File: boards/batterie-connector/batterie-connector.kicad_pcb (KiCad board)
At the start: 2 copper layers, 43 x 23 mm, 5 parts, among them J101 2W2C, J102 +, J103 -, J104 +, J105 -

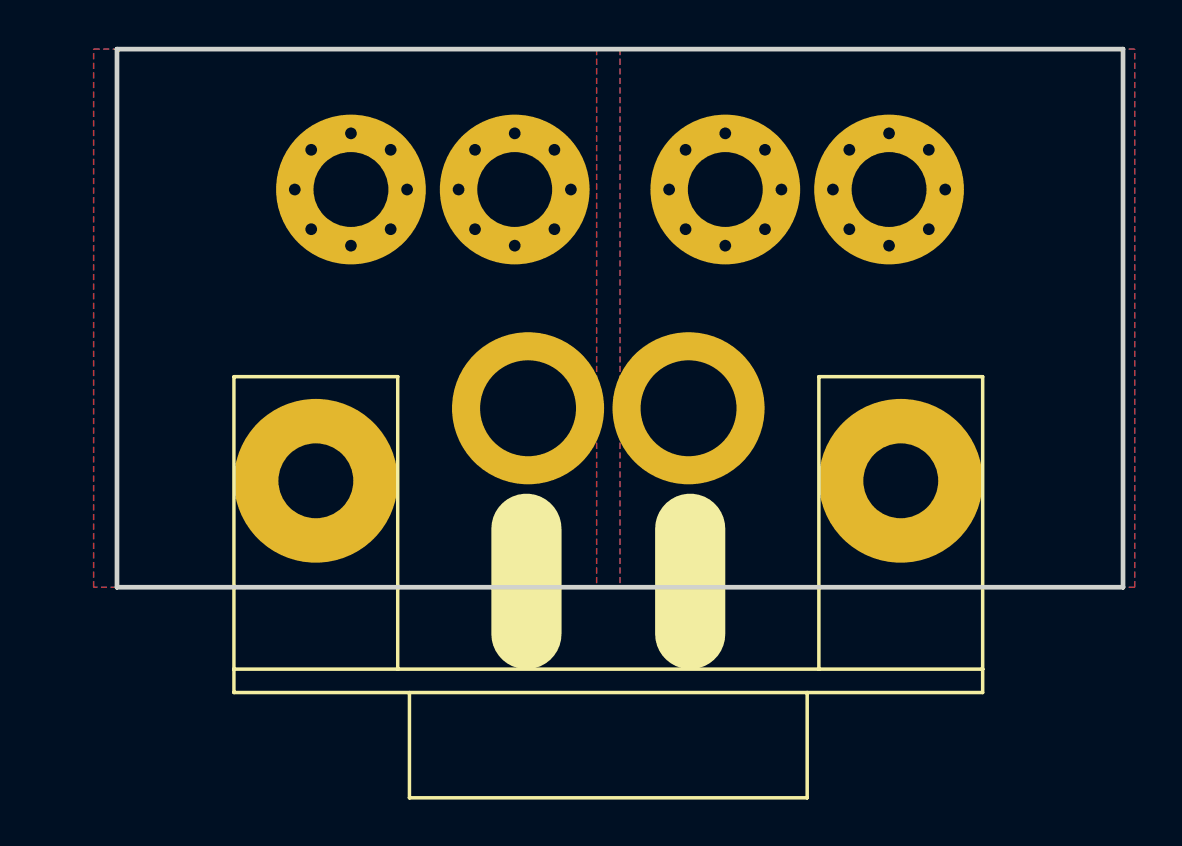
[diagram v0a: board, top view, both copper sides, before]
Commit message: [board][batterie-connector-board] rev2: more compact, silkscreen
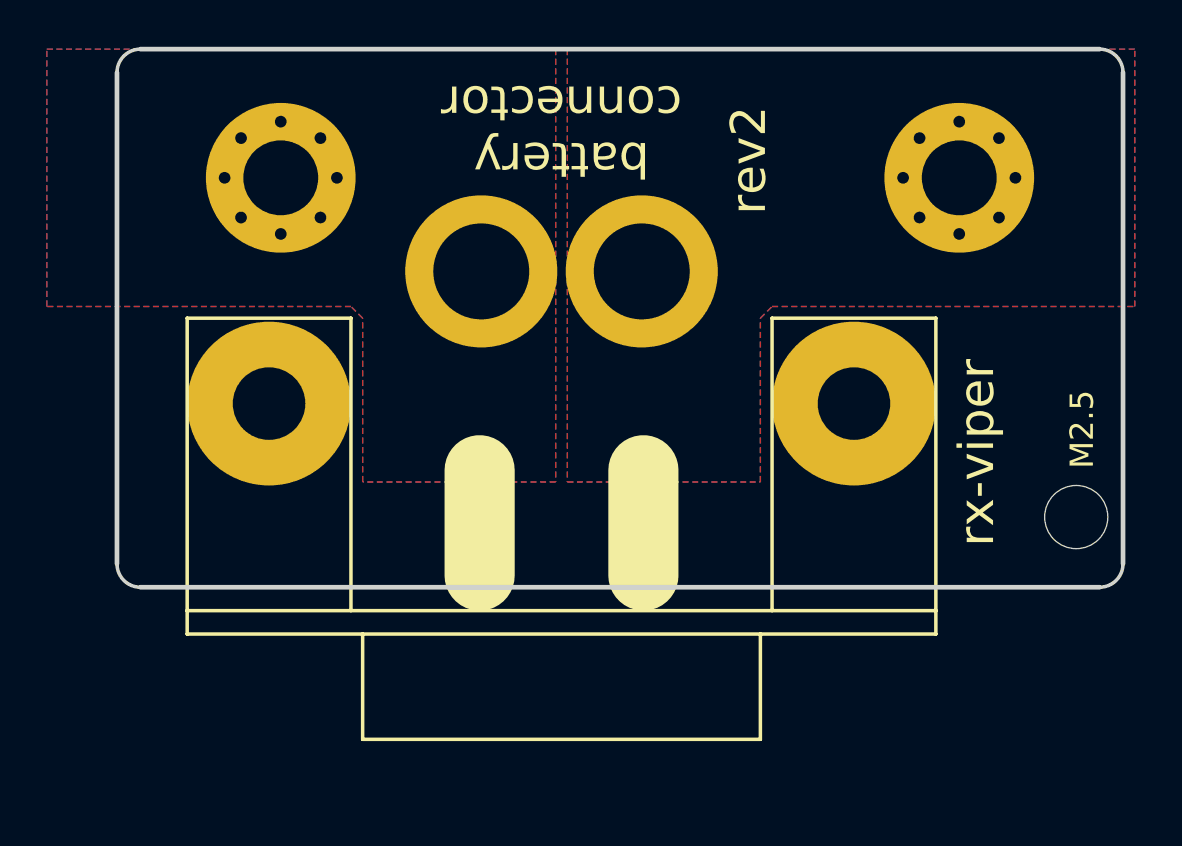
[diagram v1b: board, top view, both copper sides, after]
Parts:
- removed J104: +, MountingHole:MountingHole_3.2mm_M3_Pad_Via
- removed J105: -, MountingHole:MountingHole_3.2mm_M3_Pad_Via
- added H101: M2.5, MountingHole:MountingHole_2.7mm_M2.5_DIN965, F.Cu at (161.0, 80.0)
- moved J102 10.0 mm to (127.0, 65.5)
- moved J103 10.0 mm to (156.0, 65.5)
- moved J101 3.20 mm to (139.0, 84.5)
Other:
- outline, holes or cut-outs redrawn
- board text added: "battery connector"
- board text added: "rev2"
- board text added: "rx-viper"

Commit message: [board][batterie-connector-board] rev3: minor changes
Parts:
- moved J102 1.00 mm to (128.0, 65.5)
- moved J103 1.00 mm to (155.0, 65.5)
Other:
- board text added: "rev3"
- board text removed: "rev2"
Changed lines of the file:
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@@
   )
   (page A4)
+  (title_block
+    (title Battery-Connector)
+    (date 2019-01-01)
+    (rev rev3)
+    (company VIPER)
+  )
   (layers
     (0 F.Cu signal)
@@
   )
   (module MountingHole:MountingHole_3.2mm_M3_Pad_Via (layer F.Cu)
-    (at 156 65.5)
+    (at 155 65.5)
     (descr "Mounting Hole 3.2mm, M3")
     (tags "mounting hole 3.2mm m3")
@@
   )
   (module MountingHole:MountingHole_3.2mm_M3_Pad_Via (layer F.Cu)
-    (at 127 65.5)
+    (at 128 65.5)
     (descr "Mounting Hole 3.2mm, M3")
     (tags "mounting hole 3.2mm m3")
@@
     (pad 1 np_thru_hole circle (at 0 0) (size 2.7 2.7) (drill 2.7) (layers *.Cu *.Mask))
   )
-  (gr_text rev2 (at 147 64.75 90) (layer F.SilkS)
+  (dimension 12 (width 0.3) (layer Dwgs.User)
+    (gr_text "12,000 mm" (at 126 51.9) (layer Dwgs.User)
+      (effects (font (size 1.5 1.5) (thickness 0.3)))
+    )
+    (feature1 (pts (xy 132 59) (xy 132 53.413579)))
+    (feature2 (pts (xy 120 59) (xy 120 53.413579)))
+    (crossbar (pts (xy 120 54) (xy 132 54)))
+    (arrow1a (pts (xy 132 54) (xy 130.873496 54.586421)))
+    (arrow1b (pts (xy 132 54) (xy 130.873496 53.413579)))
+    (arrow2a (pts (xy 120 54) (xy 121.126504 54.586421)))
+    (arrow2b (pts (xy 120 54) (xy 121.126504 53.413579)))
+  )
+  (gr_text rev3 (at 147 64.75 90) (layer F.SilkS)
     (effects (font (size 1.5 1.5) (thickness 0.3)))
   )
@@
   (gr_text rx-viper (at 156.75 77.25 90) (layer F.SilkS)
     (effects (font (size 1.5 1.5) (thickness 0.3)))
-  )
-  (dimension 13 (width 0.3) (layer Dwgs.User)
-    (gr_text "13,000 mm" (at 126.5 51.9) (layer Dwgs.User)
-      (effects (font (size 1.5 1.5) (thickness 0.3)))
-    )
-    (feature1 (pts (xy 133 59) (xy 133 53.413579)))
-    (feature2 (pts (xy 120 59) (xy 120 53.413579)))
-    (crossbar (pts (xy 120 54) (xy 133 54)))
-    (arrow1a (pts (xy 133 54) (xy 131.873496 54.586421)))
-    (arrow1b (pts (xy 133 54) (xy 131.873496 53.413579)))
-    (arrow2a (pts (xy 120 54) (xy 121.126504 54.586421)))
-    (arrow2b (pts (xy 120 54) (xy 121.126504 53.413579)))
   )
   (dimension 13 (width 0.3) (layer Dwgs.User)
@@
     (polygon
       (pts
-        (xy 139.25 60) (xy 139.25 78.5) (xy 147.5 78.5) (xy 147.5 71.5) (xy 148 71)
+        (xy 139.25 60) (xy 139.25 75) (xy 147.5 75) (xy 147.5 71.5) (xy 148 71)
         (xy 163.5 71) (xy 163.5 60)
       )
@@
     (polygon
       (pts
-        (xy 139.25 60) (xy 139.25 78.5) (xy 147.5 78.5) (xy 147.5 71.5) (xy 148 71)
+        (xy 139.25 60) (xy 139.25 75) (xy 147.5 75) (xy 147.5 71.5) (xy 148 71)
         (xy 163.5 71) (xy 163.5 60)
       )
@@
     (polygon
       (pts
-        (xy 138.75 60) (xy 138.75 78.5) (xy 130.5 78.5) (xy 130.5 71.5) (xy 130 71)
+        (xy 138.75 60) (xy 138.75 75) (xy 130.5 75) (xy 130.5 71.5) (xy 130 71)
         (xy 117 71) (xy 117 60)
       )
@@
     (polygon
       (pts
-        (xy 138.75 60) (xy 138.75 78.5) (xy 130.5 78.5) (xy 130.5 71.5) (xy 130 71)
+        (xy 138.75 60) (xy 138.75 75) (xy 130.5 75) (xy 130.5 71.5) (xy 130 71)
         (xy 117 71) (xy 117 60)
       )
@@
     (polygon
       (pts
-        (xy 118 59) (xy 131.5 59) (xy 131.5 70.5) (xy 118 70.5)
-      )
-    )
+        (xy 118 59) (xy 132 59) (xy 132 70.5) (xy 118 70.5)
+      )
+    )
+  )
+  (zone (net 0) (net_name "") (layer B.Mask) (hatch edge 0.508)
+    (priority 1)
+    (connect_pads yes (clearance 0.5))
+    (min_thickness 0.5)
+    (fill yes (arc_segments 16) (thermal_gap 0.508) (thermal_bridge_width 0.508))
+    (polygon
+      (pts
+        (xy 118 59) (xy 132 59) (xy 132 70.5) (xy 118 70.5)
+      )
+    )
+  )
+  (zone (net 0) (net_name "") (layer B.Mask) (hatch edge 0.508)
+    (priority 1)
+    (connect_pads yes (clearance 0.5))
+    (min_thickness 0.5)
+    (fill yes (arc_segments 16) (thermal_gap 0.508) (thermal_bridge_width 0.508))
+    (polygon
+      (pts
+        (xy 150 59) (xy 164.5 59) (xy 164.5 70.5) (xy 150 70.5)
+      )
+    )
